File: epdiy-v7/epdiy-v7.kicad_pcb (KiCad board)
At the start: 4 copper layers, 100 x 55 mm, 118 parts, among them J1 EXTENSION_HEADER, J2 ESP_HDR, J3 XF2M-3315-1A, J4 USB_HDR, J5 USB_C_Receptacle_USB2.0, J6 CONN_BAT, J7 8BIT_HEADER, Q1 MMBT3904, Q2 MMBT3904, Q3 AO3401A, U1 ED060XC5, U10 ESP32-S3-WROOM-1, U11 TP4056, U2 PCA9535PW, U3 CH340C, U4 USBLC6-2P6, U5 PCF8563T, U6 XC6206PxxxMR, U7 ED078KH6, U8 RT9080-33GJ5, U9 RSL48_4P4X4P4, Y1 32.768K

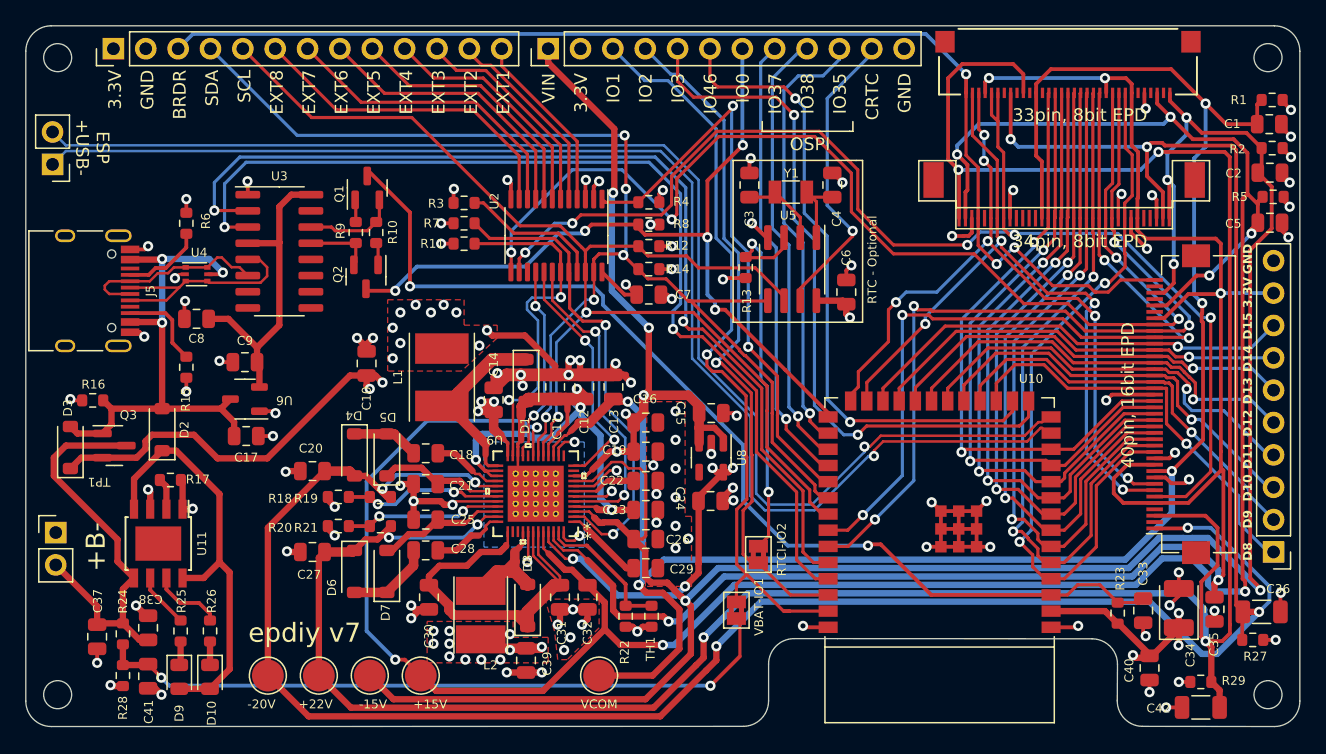
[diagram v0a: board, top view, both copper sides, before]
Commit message: fix / roll back mangled v7 pcb
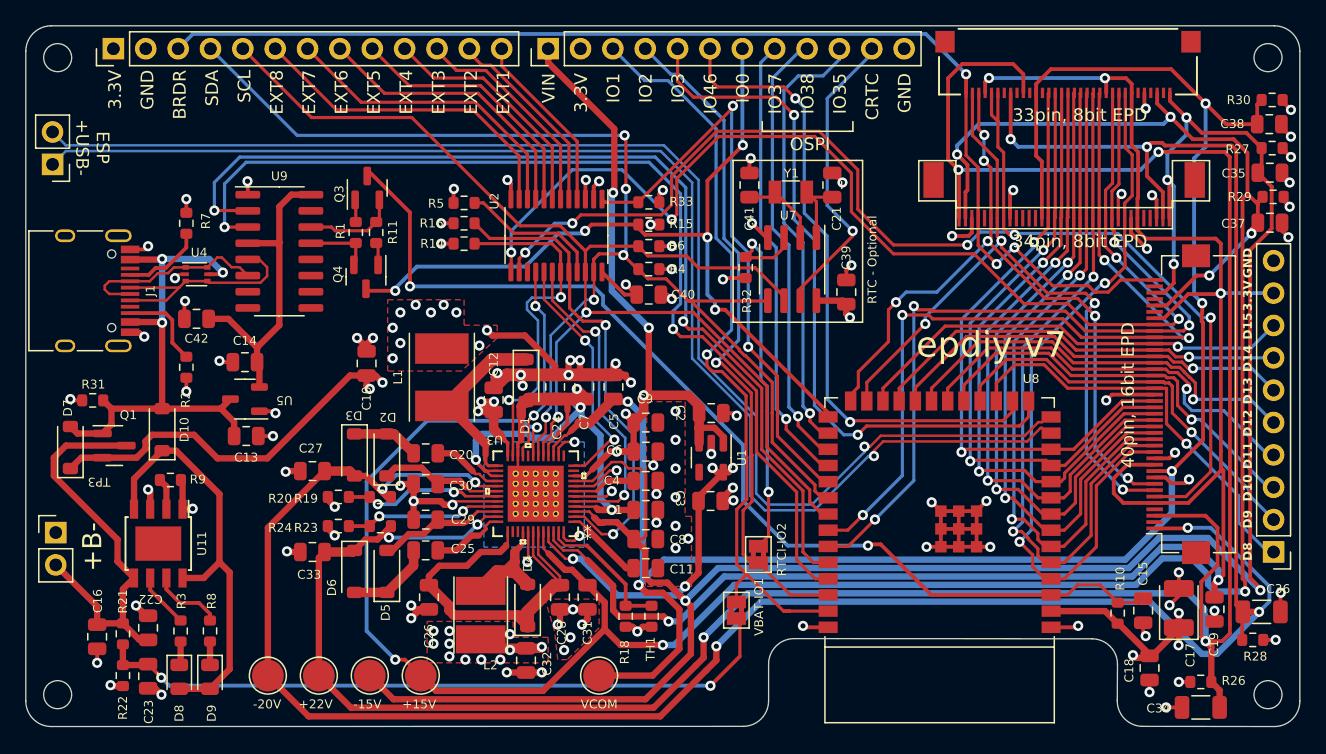
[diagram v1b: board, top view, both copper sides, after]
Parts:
- renumbered C23 to C1, C29 to C11, C14 to C12, C17 to C13, C9 to C14, C33 to C15, C37 to C16, C34 to C17, C40 to C18, C35 to C19, C15 to C2, C18 to C20, C4 to C21, C38 to C22, C41 to C23, C11 to C24, C28 to C25, C30 to C26, C20 to C27, C31 to C28, C25 to C29, C24 to C3, C21 to C30, C32 to C31, C39 to C32, C27 to C33, C42 to C34, C2 to C35, C5 to C37, C1 to C38, C6 to C39, C22 to C4, C7 to C40, C3 to C41, C8 to C42, C13 to C5, C19 to C6, C12 to C7, C26 to C8, C16 to C9, D2 to D10, D5 to D2, D4 to D3, D8 to D4, D7 to D5, D3 to D7, D9 to D8, D10 to D9, H2 to H1, H3 to H2, H4 to H3, H1 to H4, J5 to J1, J1 to J2, J4 to J3, J3 to J4, J6 to J5, J7 to J6, J2 to J7, JP2 to JP1, JP1 to JP2, Q3 to Q1, Q1 to Q3, Q2 to Q4, R9 to R1, R23 to R10, R10 to R11, R11 to R14, R8 to R15, R7 to R16, R22 to R18, R15 to R2, R18 to R20, R24 to R21, R28 to R22, R21 to R23, R20 to R24, R29 to R26, R2 to R27, R27 to R28, R5 to R29, R25 to R3, R1 to R30, R16 to R31, R13 to R32, R4 to R33, R14 to R4, R3 to R5, R12 to R6, R6 to R7, R26 to R8, R17 to R9, #SYM101 to REF**, TP2 to TP1, TP3 to TP2, TP1 to TP3, U8 to U1, U1 to U10, U9 to U3, U6 to U5, U7 to U6, U5 to U7, U10 to U8, U3 to U9
